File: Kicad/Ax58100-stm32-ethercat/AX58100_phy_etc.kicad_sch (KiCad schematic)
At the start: 46 parts, among them U3 AMS1117-1.2

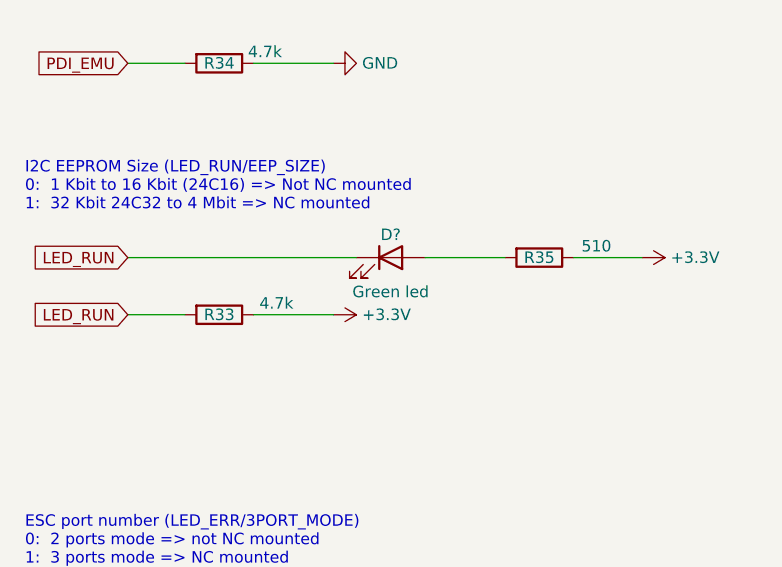
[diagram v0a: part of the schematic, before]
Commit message: Steppers, encoders, IO, etc remapped
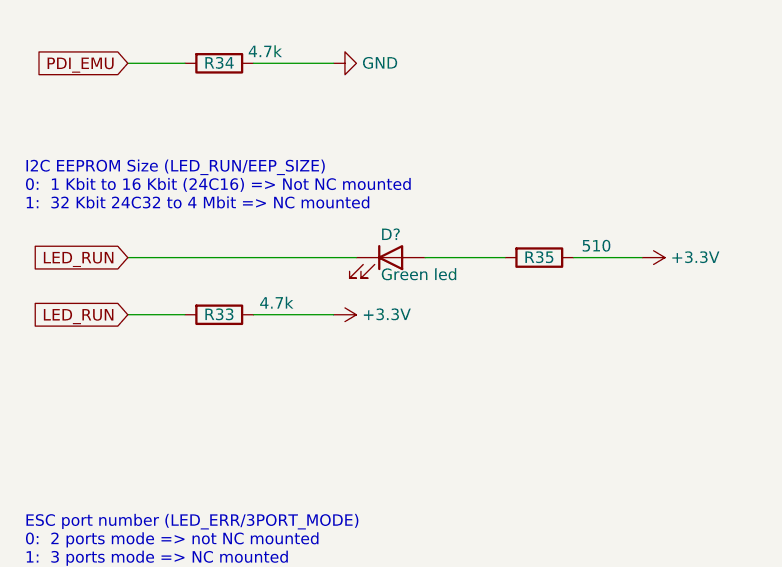
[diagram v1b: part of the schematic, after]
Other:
- title: (none) -> MetalMusings EaserCAT 3000
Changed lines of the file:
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@@
 (kicad_sch (version 20230121) (generator eeschema)
   (paper "A4")
+  (title_block
+    (title "MetalMusings EaserCAT 3000")
+  )
   (junction (at 236.22 123.19) (diameter 0) (color 0 0 0 0)
   )
@@
       (effects (font (size 1.27 1.27)))
     )
-    (property "Value" "Green led" (at 228.6 53.34 0)
-      (effects (font (size 1.27 1.27)))
-    )
+    (property "Value" "Green led" (at 231.775 51.435 0)
+      (effects (font (size 1.27 1.27)))
+    )

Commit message: wip
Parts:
- renumbered B7 to B1, B6 to B2, B5 to B3, B2 to B4, B1 to B5, B4 to B6, B3 to B7, C10 to C24, C9 to C25, C8 to C26, C7 to C27, C6 to C28, C5 to C29, C4 to C30, C3 to C31, C2 to C32, C1 to C33, R35 to R14, R43 to R20, R33 to R27, R34 to R28, R17 to R29, R16 to R30, R15 to R31, R14 to R32, R13 to R33, R12 to R34, R11 to R35, R10 to R36, R7 to R39, R6 to R40, R5 to R41, R4 to R42, R28 to R43, R20 to R49, R19 to R50

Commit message: Might be in final shape.
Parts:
- renumbered B4 to B2, B5 to B3, B2 to B4, B3 to B5, C24 to C28, C25 to C29, C26 to C30, C27 to C31, C28 to C32, C29 to C33, C30 to C34, C31 to C35, C32 to C36, C33 to C37, R28 to R45, R27 to R47, R29 to R48, R30 to R49, R31 to R50, R32 to R51, R33 to R52, R34 to R53, R35 to R54, R36 to R55, R14 to R56, R39 to R58, R40 to R59, R41 to R60, R42 to R61, R20 to R62, R43 to R63, R49 to R69, R50 to R70

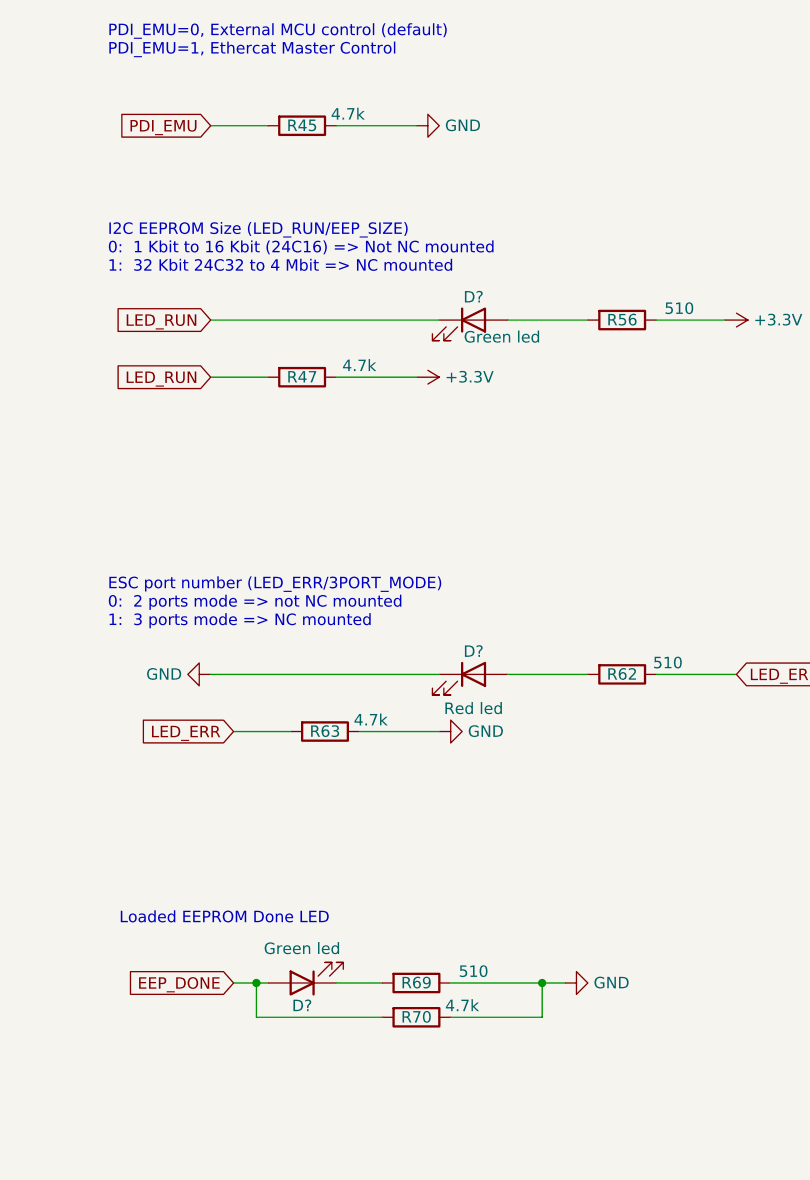
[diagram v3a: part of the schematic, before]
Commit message: 4.7k to 4k7
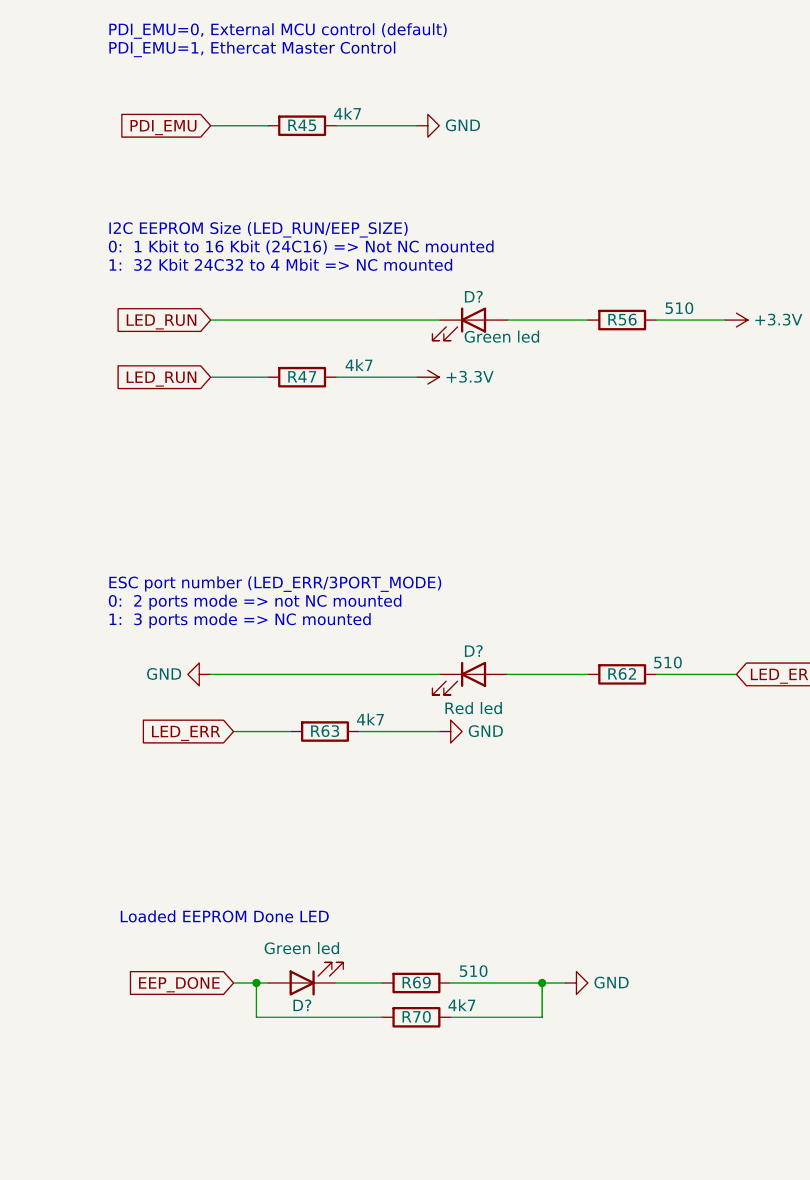
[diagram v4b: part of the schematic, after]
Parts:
- R45, R47, R63, R70: value 4.7k -> 4k7
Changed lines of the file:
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@@
       (effects (font (size 1.27 1.27)))
     )
-    (property "Value" "4.7k" (at 227.33 125.73 90)
+    (property "Value" "4k7" (at 227.33 125.73 90)
       (effects (font (size 1.27 1.27)))
     )
@@
       (effects (font (size 1.27 1.27)))
     )
-    (property "Value" "4.7k" (at 217.17 93.98 90)
+    (property "Value" "4k7" (at 217.17 93.98 90)
       (effects (font (size 1.27 1.27)))
     )
@@
       (effects (font (size 1.27 1.27)))
     )
-    (property "Value" "4.7k" (at 214.63 26.67 90)
+    (property "Value" "4k7" (at 214.63 26.67 90)
       (effects (font (size 1.27 1.27)))
     )
@@
       (effects (font (size 1.27 1.27)))
     )
-    (property "Value" "4.7k" (at 215.9 54.61 90)
-      (effects (font (size 1.27 1.27)))
-    )
+    (property "Value" "4k7" (at 215.9 54.61 90)
+      (effects (font (size 1.27 1.27)))
+    )

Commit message: all leds are now 0603
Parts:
- D? (x3): footprint LED_SMD:LED_0805_2012Metric -> LED_SMD:LED_0603_1608Metric
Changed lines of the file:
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@@
       (effects (font (size 1.27 1.27)))
     )
-    (property "Footprint" "LED_SMD:LED_0805_2012Metric" (at 209.55 123.19 0)
+    (property "Footprint" "LED_SMD:LED_0603_1608Metric" (at 209.55 123.19 0)
       (effects (font (size 1.27 1.27)) hide)
     )
@@
       (effects (font (size 1.27 1.27)))
     )
-    (property "Footprint" "LED_SMD:LED_0805_2012Metric" (at 228.6 49.53 0)
+    (property "Footprint" "LED_SMD:LED_0603_1608Metric" (at 228.6 49.53 0)
       (effects (font (size 1.27 1.27)) hide)
     )
@@
       (effects (font (size 1.27 1.27)))
     )
-    (property "Footprint" "LED_SMD:LED_0805_2012Metric" (at 228.6 88.9 0)
-      (effects (font (size 1.27 1.27)) hide)
-    )
+    (property "Footprint" "LED_SMD:LED_0603_1608Metric" (at 228.6 88.9 0)
+      (effects (font (size 1.27 1.27)) hide)
+    )

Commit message: Getting ready for fab
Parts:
- renumbered R45 to R46, R47 to R48, R48 to R49, R49 to R50, R50 to R51, R51 to R52, R52 to R53, R53 to R54, R54 to R55, R55 to R56, R56 to R57, R58 to R59, R59 to R60, R60 to R61, R61 to R62, R62 to R63, R63 to R64, R69 to R70, R70 to R71
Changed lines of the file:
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@@
   (symbol (lib_id "Device:R") (at 245.11 88.9 270) (unit 1)
     (in_bom yes) (on_board yes) (dnp no)
-    (property "Reference" "R62" (at 245.11 88.9 90)
+    (property "Reference" "R63" (at 245.11 88.9 90)
       (effects (font (size 1.27 1.27)))
     )
@@
       (project "Ax58100-stm32-ethercat"
         (path "/5597aedc-b607-407f-bbfd-31b3b298ecb1/5bf93325-f5d9-4344-9bf3-f5fc91bc1622"
-          (reference "R62") (unit 1)
+          (reference "R63") (unit 1)
         )
       )
@@
   (symbol (lib_id "Device:R") (at 222.25 127 270) (unit 1)
     (in_bom yes) (on_board yes) (dnp no)
-    (property "Reference" "R70" (at 222.25 127 90)
+    (property "Reference" "R71" (at 222.25 127 90)
       (effects (font (size 1.27 1.27)))
     )
@@
       (project "Ax58100-stm32-ethercat"
         (path "/5597aedc-b607-407f-bbfd-31b3b298ecb1/5bf93325-f5d9-4344-9bf3-f5fc91bc1622"
-          (reference "R70") (unit 1)
+          (reference "R71") (unit 1)
         )
       )
@@
   (symbol (lib_id "Device:R") (at 46.99 36.83 180) (unit 1)
     (in_bom yes) (on_board yes) (dnp no)
-    (property "Reference" "R54" (at 46.99 36.83 90)
+    (property "Reference" "R55" (at 46.99 36.83 90)
       (effects (font (size 1.27 1.27)))
     )
@@
       (project "Ax58100-stm32-ethercat"
         (path "/5597aedc-b607-407f-bbfd-31b3b298ecb1/5bf93325-f5d9-4344-9bf3-f5fc91bc1622"
-          (reference "R54") (unit 1)
+          (reference "R55") (unit 1)
         )
       )
@@
   (symbol (lib_id "Device:R") (at 52.07 36.83 180) (unit 1)
     (in_bom yes) (on_board yes) (dnp no)
-    (property "Reference" "R53" (at 52.07 36.83 90)
+    (property "Reference" "R54" (at 52.07 36.83 90)
       (effects (font (size 1.27 1.27)))
     )
@@
       (project "Ax58100-stm32-ethercat"
         (path "/5597aedc-b607-407f-bbfd-31b3b298ecb1/5bf93325-f5d9-4344-9bf3-f5fc91bc1622"
-          (reference "R53") (unit 1)
+          (reference "R54") (unit 1)
         )
       )
@@
   (symbol (lib_id "Device:R") (at 135.89 59.69 0) (unit 1)
     (in_bom yes) (on_board yes) (dnp no)
-    (property "Reference" "R61" (at 135.89 59.69 90)
+    (property "Reference" "R62" (at 135.89 59.69 90)
       (effects (font (size 1.27 1.27)))
     )
@@
       (project "Ax58100-stm32-ethercat"
         (path "/5597aedc-b607-407f-bbfd-31b3b298ecb1/5bf93325-f5d9-4344-9bf3-f5fc91bc1622"
-          (reference "R61") (unit 1)
+          (reference "R62") (unit 1)
         )
       )
@@
   (symbol (lib_id "Device:R") (at 245.11 49.53 270) (unit 1)
     (in_bom yes) (on_board yes) (dnp no)
-    (property "Reference" "R56" (at 245.11 49.53 90)
+    (property "Reference" "R57" (at 245.11 49.53 90)
       (effects (font (size 1.27 1.27)))
     )
@@
       (project "Ax58100-stm32-ethercat"
         (path "/5597aedc-b607-407f-bbfd-31b3b298ecb1/5bf93325-f5d9-4344-9bf3-f5fc91bc1622"
-          (reference "R56") (unit 1)
+          (reference "R57") (unit 1)
         )
       )
@@
   (symbol (lib_id "Device:R") (at 48.26 96.52 180) (unit 1)
     (in_bom yes) (on_board yes) (dnp no)
-    (property "Reference" "R50" (at 48.26 96.52 90)
+    (property "Reference" "R51" (at 48.26 96.52 90)
       (effects (font (size 1.27 1.27)))
     )
@@
       (project "Ax58100-stm32-ethercat"
         (path "/5597aedc-b607-407f-bbfd-31b3b298ecb1/5bf93325-f5d9-4344-9bf3-f5fc91bc1622"
-          (reference "R50") (unit 1)
+          (reference "R51") (unit 1)
         )
       )
@@
   (symbol (lib_id "Device:R") (at 212.09 95.25 270) (unit 1)
     (in_bom yes) (on_board yes) (dnp no)
-    (property "Reference" "R63" (at 212.09 95.25 90)
+    (property "Reference" "R64" (at 212.09 95.25 90)
       (effects (font (size 1.27 1.27)))
     )
@@
       (project "Ax58100-stm32-ethercat"
         (path "/5597aedc-b607-407f-bbfd-31b3b298ecb1/5bf93325-f5d9-4344-9bf3-f5fc91bc1622"
-          (reference "R63") (unit 1)
+          (reference "R64") (unit 1)
         )
       )
@@
   (symbol (lib_id "Device:R") (at 209.55 27.94 270) (unit 1)
     (in_bom yes) (on_board yes) (dnp no)
-    (property "Reference" "R45" (at 209.55 27.94 90)
+    (property "Reference" "R46" (at 209.55 27.94 90)
       (effects (font (size 1.27 1.27)))
     )
@@
       (project "Ax58100-stm32-ethercat"
         (path "/5597aedc-b607-407f-bbfd-31b3b298ecb1/5bf93325-f5d9-4344-9bf3-f5fc91bc1622"
-          (reference "R45") (unit 1)
+          (reference "R46") (unit 1)
         )
       )
@@
   (symbol (lib_id "Device:R") (at 41.91 36.83 180) (unit 1)
     (in_bom yes) (on_board yes) (dnp no)
-    (property "Reference" "R55" (at 41.91 36.83 90)
+    (property "Reference" "R56" (at 41.91 36.83 90)
       (effects (font (size 1.27 1.27)))
     )
@@
       (project "Ax58100-stm32-ethercat"
         (path "/5597aedc-b607-407f-bbfd-31b3b298ecb1/5bf93325-f5d9-4344-9bf3-f5fc91bc1622"
-          (reference "R55") (unit 1)
+          (reference "R56") (unit 1)
         )
       )
@@
   (symbol (lib_id "Device:R") (at 57.15 36.83 180) (unit 1)
     (in_bom yes) (on_board yes) (dnp no)
-    (property "Reference" "R52" (at 57.15 36.83 90)
+    (property "Reference" "R53" (at 57.15 36.83 90)
       (effects (font (size 1.27 1.27)))
     )
@@
       (project "Ax58100-stm32-ethercat"
         (path "/5597aedc-b607-407f-bbfd-31b3b298ecb1/5bf93325-f5d9-4344-9bf3-f5fc91bc1622"
-          (reference "R52") (unit 1)
+          (reference "R53") (unit 1)
         )
       )
@@
   (symbol (lib_id "Device:R") (at 222.25 123.19 270) (unit 1)
     (in_bom yes) (on_board yes) (dnp no)
-    (property "Reference" "R69" (at 222.25 123.19 90)
+    (property "Reference" "R70" (at 222.25 123.19 90)
       (effects (font (size 1.27 1.27)))
     )
@@
       (project "Ax58100-stm32-ethercat"
         (path "/5597aedc-b607-407f-bbfd-31b3b298ecb1/5bf93325-f5d9-4344-9bf3-f5fc91bc1622"
-          (reference "R69") (unit 1)
+          (reference "R70") (unit 1)
         )
       )
@@
   (symbol (lib_id "Device:R") (at 53.34 96.52 180) (unit 1)
     (in_bom yes) (on_board yes) (dnp no)
-    (property "Reference" "R49" (at 53.34 96.52 90)
+    (property "Reference" "R50" (at 53.34 96.52 90)
       (effects (font (size 1.27 1.27)))
     )
@@
       (project "Ax58100-stm32-ethercat"
         (path "/5597aedc-b607-407f-bbfd-31b3b298ecb1/5bf93325-f5d9-4344-9bf3-f5fc91bc1622"
-          (reference "R49") (unit 1)
+          (reference "R50") (unit 1)
         )
       )
@@
   (symbol (lib_id "Device:R") (at 209.55 55.88 270) (unit 1)
     (in_bom yes) (on_board yes) (dnp no)
-    (property "Reference" "R47" (at 209.55 55.88 90)
+    (property "Reference" "R48" (at 209.55 55.88 90)
       (effects (font (size 1.27 1.27)))
     )
@@
       (project "Ax58100-stm32-ethercat"
         (path "/5597aedc-b607-407f-bbfd-31b3b298ecb1/5bf93325-f5d9-4344-9bf3-f5fc91bc1622"
-          (reference "R47") (unit 1)
+          (reference "R48") (unit 1)
         )
       )
@@
   (symbol (lib_id "Device:R") (at 43.18 96.52 180) (unit 1)
     (in_bom yes) (on_board yes) (dnp no)
-    (property "Reference" "R51" (at 43.18 96.52 90)
+    (property "Reference" "R52" (at 43.18 96.52 90)
       (effects (font (size 1.27 1.27)))
     )
@@
       (project "Ax58100-stm32-ethercat"
         (path "/5597aedc-b607-407f-bbfd-31b3b298ecb1/5bf93325-f5d9-4344-9bf3-f5fc91bc1622"
-          (reference "R51") (unit 1)
+          (reference "R52") (unit 1)
         )
       )
@@
   (symbol (lib_id "Device:R") (at 130.81 48.26 270) (unit 1)
     (in_bom yes) (on_board yes) (dnp no)
-    (property "Reference" "R60" (at 130.81 48.26 90)
+    (property "Reference" "R61" (at 130.81 48.26 90)
       (effects (font (size 1.27 1.27)))
     )
@@
       (project "Ax58100-stm32-ethercat"
         (path "/5597aedc-b607-407f-bbfd-31b3b298ecb1/5bf93325-f5d9-4344-9bf3-f5fc91bc1622"
-          (reference "R60") (unit 1)
+          (reference "R61") (unit 1)
         )
       )
@@
   (symbol (lib_id "Device:R") (at 58.42 96.52 180) (unit 1)
     (in_bom yes) (on_board yes) (dnp no)
-    (property "Reference" "R48" (at 58.42 96.52 90)
+    (property "Reference" "R49" (at 58.42 96.52 90)
       (effects (font (size 1.27 1.27)))
     )
@@
       (project "Ax58100-stm32-ethercat"
         (path "/5597aedc-b607-407f-bbfd-31b3b298ecb1/5bf93325-f5d9-4344-9bf3-f5fc91bc1622"
-          (reference "R48") (unit 1)
+          (reference "R49") (unit 1)
         )
       )
@@
   (symbol (lib_id "Device:R") (at 133.35 107.95 270) (unit 1)
     (in_bom yes) (on_board yes) (dnp no)
-    (property "Reference" "R58" (at 133.35 107.95 90)
+    (property "Reference" "R59" (at 133.35 107.95 90)
       (effects (font (size 1.27 1.27)))
     )
@@
       (project "Ax58100-stm32-ethercat"
         (path "/5597aedc-b607-407f-bbfd-31b3b298ecb1/5bf93325-f5d9-4344-9bf3-f5fc91bc1622"
-          (reference "R58") (unit 1)
+          (reference "R59") (unit 1)
         )
       )
@@
   (symbol (lib_id "Device:R") (at 138.43 119.38 0) (unit 1)
     (in_bom yes) (on_board yes) (dnp no)
-    (property "Reference" "R59" (at 138.43 119.38 90)
+    (property "Reference" "R60" (at 138.43 119.38 90)
       (effects (font (size 1.27 1.27)))
     )
@@
       (project "Ax58100-stm32-ethercat"
         (path "/5597aedc-b607-407f-bbfd-31b3b298ecb1/5bf93325-f5d9-4344-9bf3-f5fc91bc1622"
-          (reference "R59") (unit 1)
-        )
-      )
+          (reference "R60") (unit 1)
+        )
+      )
